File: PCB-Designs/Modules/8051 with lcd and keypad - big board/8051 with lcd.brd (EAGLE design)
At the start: 6.9 x 7 mm, 31 parts, among them IC1 AT89S51, IC2 7805TV

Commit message: change
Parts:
- removed CONNECTOR-1, CONNECTOR3: 8 pin, con-amp-quick:08P
- removed SL1: keypad, con-amp-quick:10P
- added S10, S11, S12, S13, S14, S15, S16, S17, S18, S5, S6, S7, S8, S9: (no value), switch-dil:DP-02
- added S3, S4: push switch, switch-dil:DP-02
- moved LED2 97.6 mm to (-10.2, 72.4)
- moved R2 96.0 mm to (-22.9, 72.4)
- moved CONNECTOR-5 58.5 mm to (3.81, 1.27), turned to 180 degrees
- moved CONN-7 55.4 mm to (-16.5, -12.7), turned to 180 degrees
- moved AVRCONNECTOR 51.6 mm to (12.7, 48.3)
- moved SL8 51.6 mm to (8.89, 48.3)
- moved CONN-6 38.9 mm to (-16.5, 0.00)
- moved C6 36.9 mm to (101.6, -7.62)
- moved BRIDGE 34.1 mm to (3.81, 16.5)
- moved RN 30.6 mm to (39.4, 30.5), turned to 180 degrees
- moved R1 29.3 mm to (90.2, 8.89)
- moved VR 24.3 mm to (125.7, -19.1), turned to 90 degrees
- moved J1 16.2 mm to (-16.5, 33.0)
- moved JP1 14.8 mm to (-15.2, 14.0), turned to 180 degrees
- moved S2 14.5 mm to (90.2, -2.54)
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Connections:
- new net N$22: S16.1
- new net N$3: S3.2, S4.2, S5.2, S6.2
- new net N$33: S3.1, S7.4
- new net N$34: S11.4, S7.1
- new net N$36: S11.1, S15.4
- new net N$37: S12.4, S8.1
- new net N$40: S12.1, S16.4
- new net N$44: S13.1, S17.4
- new net N$49: S14.1, S18.4
- new net N$50: S10.1, S14.4
- new net N$62: S4.1, S8.4
- new net N$63: S5.1, S9.4
- new net N$64: S10.4, S6.1
- new net N$65: S13.4, S9.1
- net N$15: now also AVRCONNECTOR.5, IC1.6, RN.4; no longer AVRCONNECTOR.1, CONNECTOR3.2, IC1.7, RN.3, SL1.4
- net N$17: now also S15.1; no longer CONNECTOR3.4, SL1.6
- net N$18: now also S15.2, S16.2, S17.2, S18.2; no longer CONNECTOR3.5, SL1.7
- net N$19: now also S11.2, S12.2, S13.2, S14.2; no longer CONNECTOR3.6, SL1.8
- net N$20: now also S10.2, S7.2, S8.2, S9.2; no longer CONNECTOR3.7, SL1.9
- net N$21: no longer CONNECTOR3.8, SL1.10
- net N$30: no longer CONNECTOR-1.1
- net N$31: no longer CONNECTOR-1.2
- net N$32: no longer CONNECTOR-1.3
- net N$35: no longer CONNECTOR-1.6
- net N$39: no longer SL1.2
- net N$41: no longer SL1.1
- net N$42: now also AVRCONNECTOR.1, IC1.7, RN.3, S17.1; no longer AVRCONNECTOR.5, CONNECTOR3.3, IC1.6, RN.4, SL1.5
- net N$45: now also S18.1; no longer CONNECTOR3.1, SL1.3
- net N$51: no longer CONNECTOR-1.4
- net N$52: no longer CONNECTOR-1.5
- net N$54: no longer CONNECTOR-1.7
- net N$55: no longer CONNECTOR-1.8
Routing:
- net N$3: track 477.5 -> 42.2 mm
- net N$39: track 409.5 -> 830.3 mm
- net N$14: track 79.0 -> 329.9 mm
- net N$15: track 71.0 -> 206.8 mm
- net N$45: track 74.6 -> 162.9 mm
- net N$20: track 46.3 -> 128.7 mm
- net N$5: track 55.8 -> 131.9 mm
- net N$18: track 53.5 -> 125.9 mm
- net N$19: track 49.9 -> 121.1 mm
- net N$21: track 42.7 -> 7.62 mm
- net N$41: track 532.1 -> 502.0 mm
- net N$58: track 100.0 -> 121.6 mm
- net N$47: track 35.2 -> 56.2 mm
- net N$17: track 57.1 -> 36.5 mm
- net N$50: track 0.00 -> 18.4 mm
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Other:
- outline, holes or cut-outs redrawn

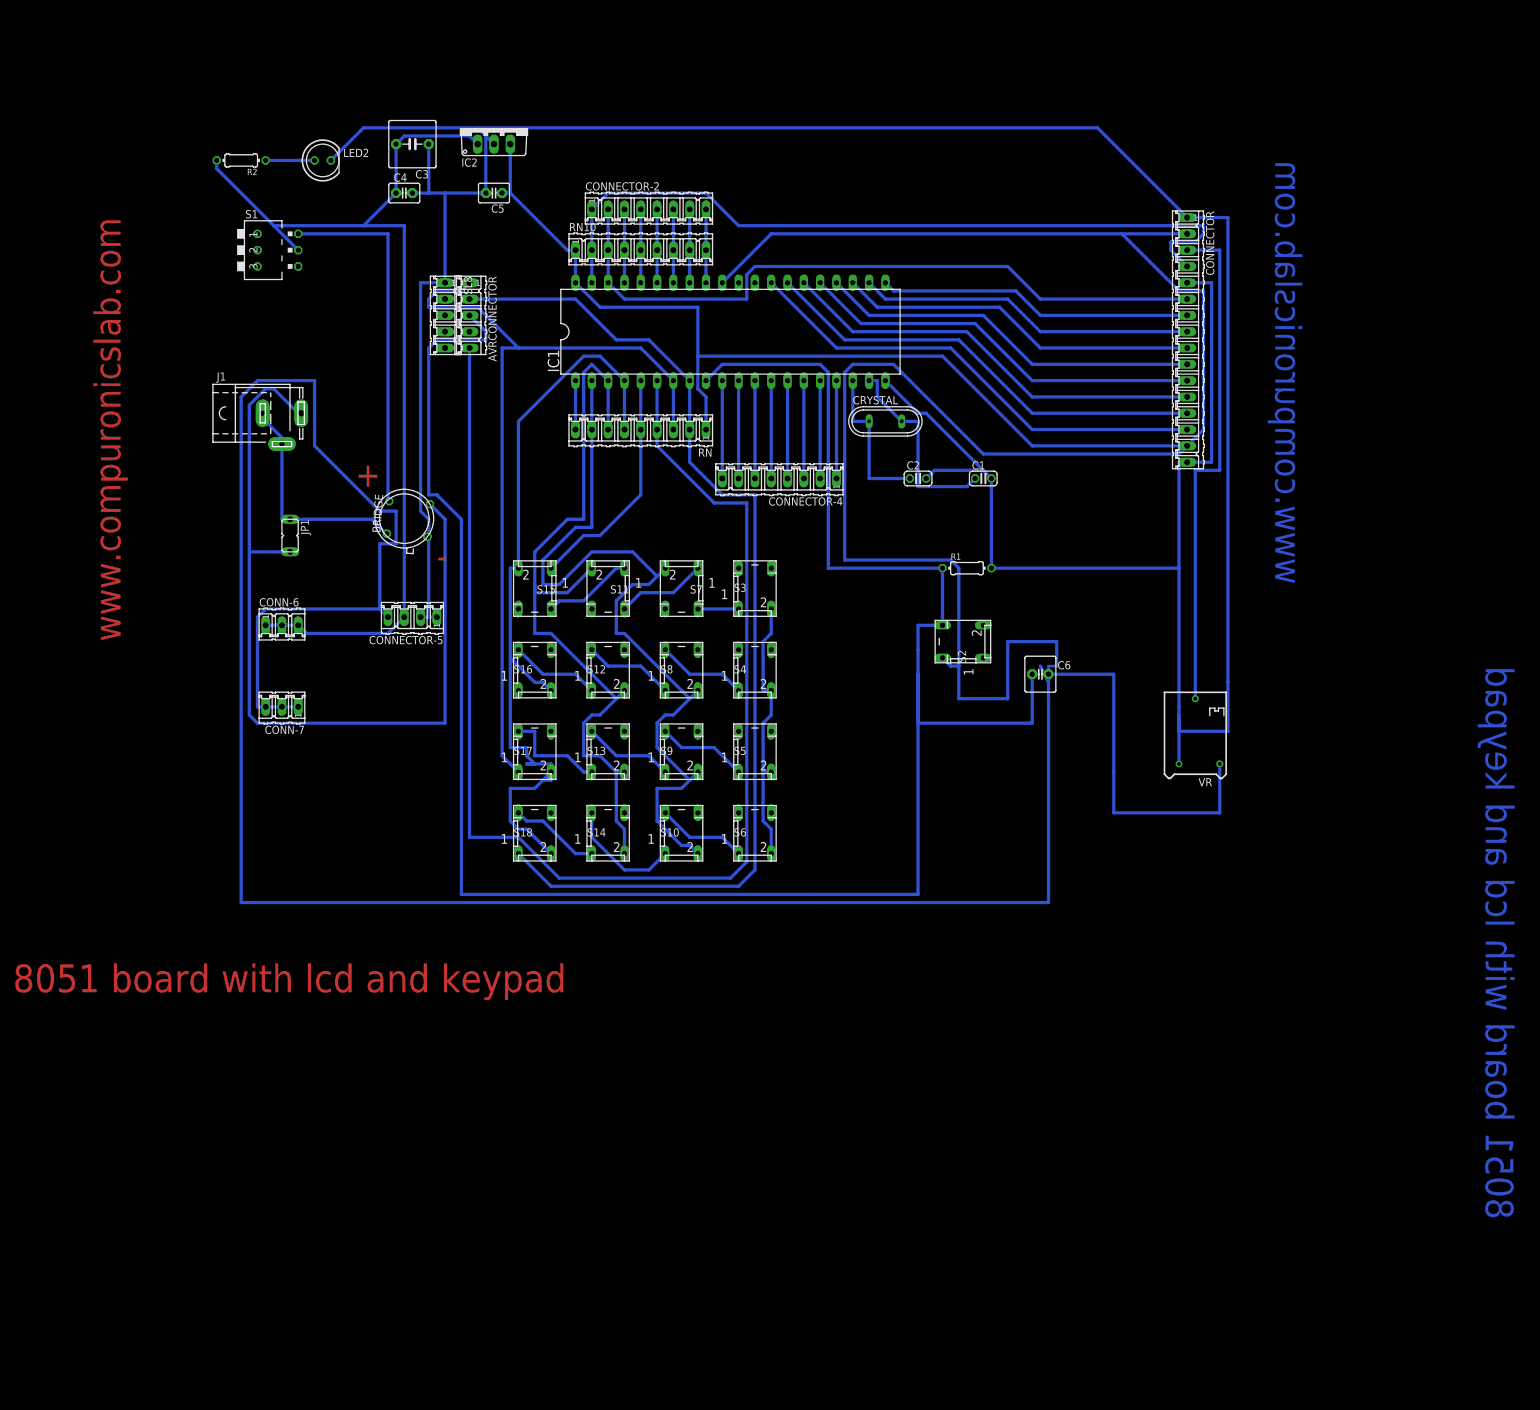
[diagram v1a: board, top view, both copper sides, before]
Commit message: 
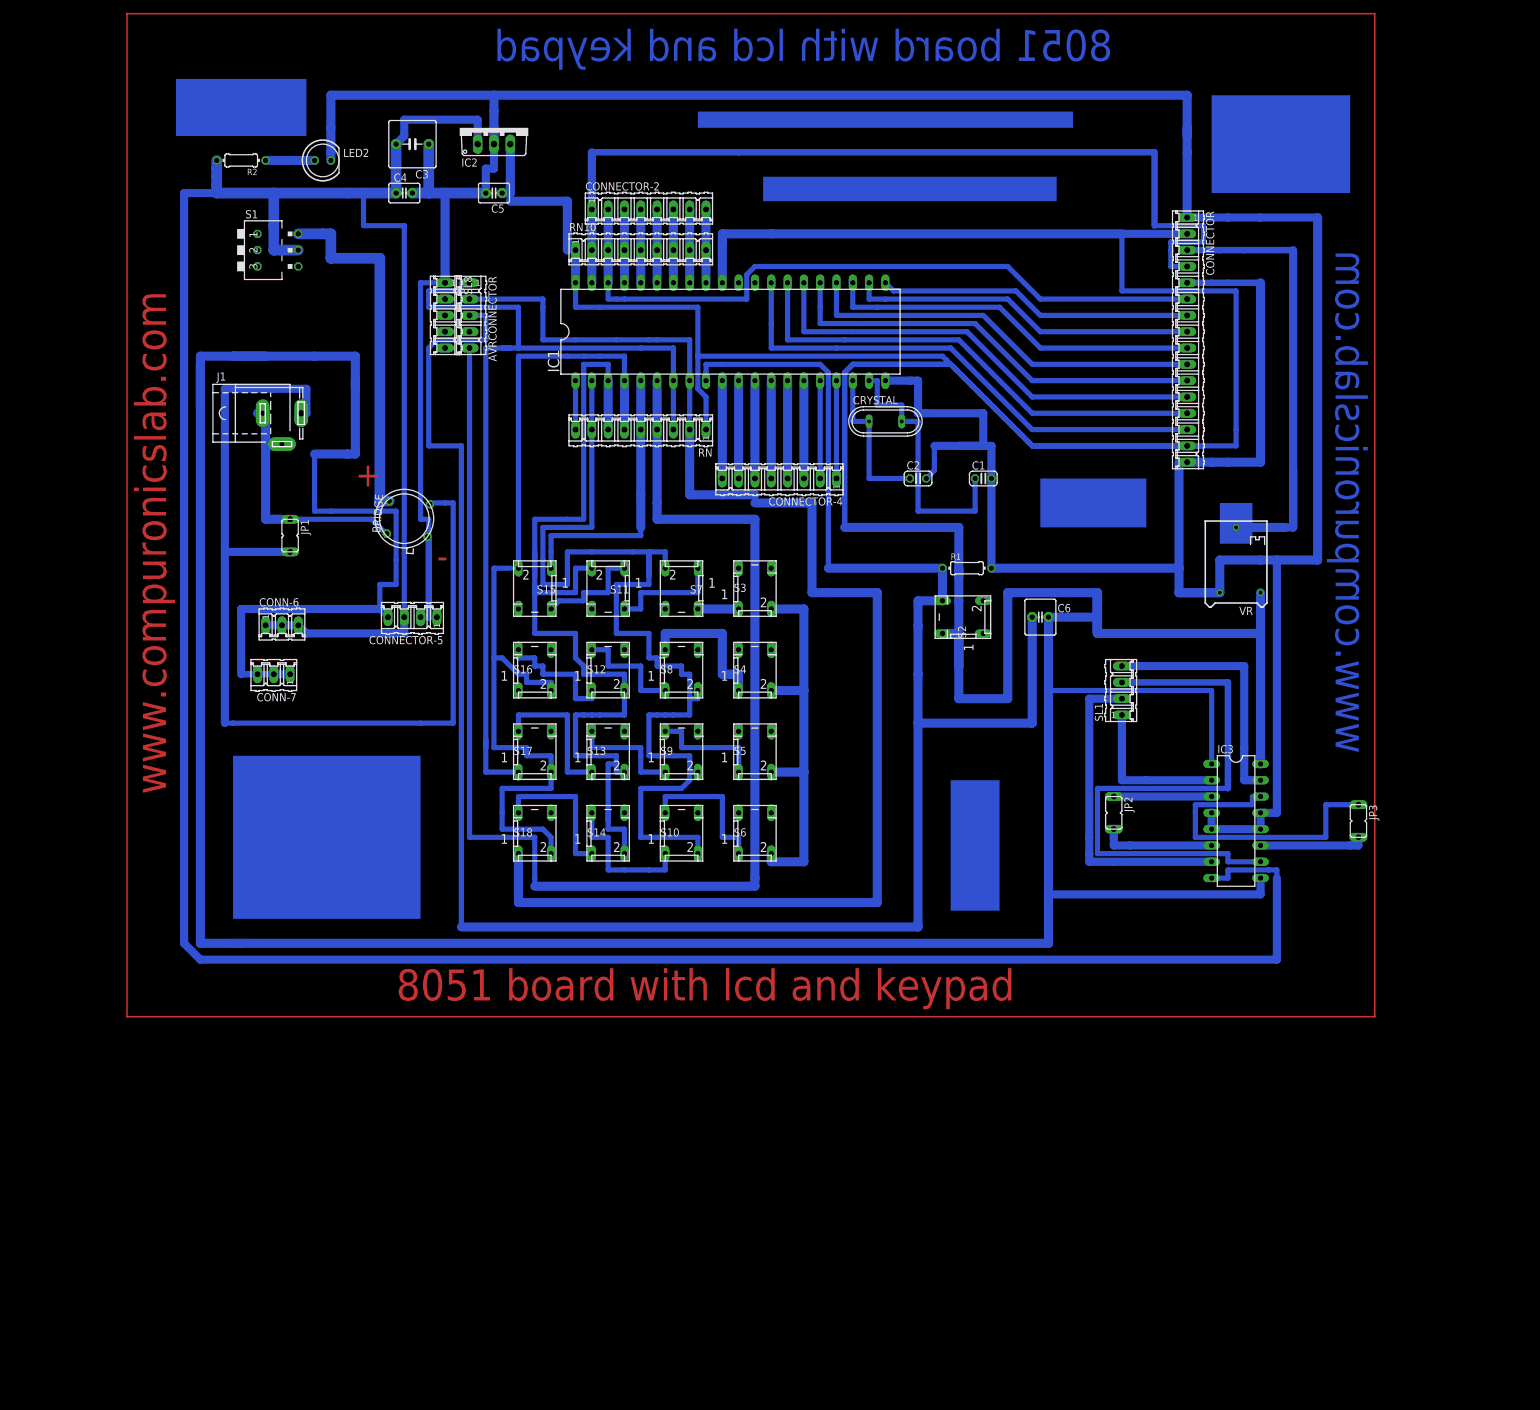
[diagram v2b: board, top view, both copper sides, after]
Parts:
- added IC3: L293D, st-microelectronics:DIL16
- added JP2, JP3: TRANSFORMER, jumper:JP1
- added SL1: (no value), con-amp-quick:04P
- moved VR 27.4 mm to (132.1, 7.62)
- moved C6 8.89 mm to (101.6, 1.27)
- moved CONN-7 5.24 mm to (-17.8, -7.62)
- moved S2 3.81 mm to (90.2, 1.27)
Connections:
- removed net N$4: C3.2, C4.1, CONN-6.1, CONN-6.2, CONN-6.3, CONNECTOR-5.3, IC2.1, R2.2, S1.5
- new net N$43: C3.2, C4.1, CONN-6.1, CONN-6.2, CONN-6.3, CONNECTOR-5.3, IC2.1, IC3.8, R2.2, S1.5
- new net N$56: BRIDGE.1, C1.2, C2.2, C3.1, C4.2, C5.2, CONNECTOR-5.1, CONNECTOR-5.2, CONNECTOR.1, CONNECTOR.16, CONNECTOR.5, IC1.20, IC2.2, IC3.12, IC3.13, IC3.4, IC3.5, LED2.K, R1.2, SL8.1, VR.3
- new net N$57: IC3.3, JP2.1
- new net N$59: IC3.6, JP2.2
- new net N$60: IC3.14, JP3.1
- new net N$61: IC3.11, JP3.2
- new net N$66: IC3.7, SL1.2
- new net N$67: IC3.10, SL1.3
- new net N$68: IC3.15, SL1.4
- net N$39: now also IC3.1, IC3.16, IC3.9
- net N$41: now also IC3.2, SL1.1; no longer BRIDGE.1, C1.2, C2.2, C3.1, C4.2, C5.2, CONNECTOR-5.1, CONNECTOR-5.2, CONNECTOR.1, CONNECTOR.16, CONNECTOR.5, IC1.20, IC2.2, LED2.K, R1.2, SL8.1, VR.3
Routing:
- net N$23: track 0.00 -> 701.0 mm
- net N$56: track 0.00 -> 613.2 mm
- net N$43: track 0.00 -> 503.8 mm
- net N$41: track 502.0 -> 24.1 mm
- net N$39: track 830.3 -> 1166.3 mm
- net N$4: track 152.2 -> 0.00 mm
- net N$67: track 0.00 -> 90.2 mm
- net N$45: track 162.9 -> 223.5 mm
- net N$66: track 0.00 -> 49.5 mm
- net N$60: track 0.00 -> 47.0 mm
- net N$20: track 128.7 -> 170.7 mm
- net N$68: track 0.00 -> 41.9 mm
- net N$19: track 121.1 -> 155.5 mm
- net N$3: track 42.2 -> 71.1 mm
- net N$42: track 128.8 -> 154.9 mm
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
